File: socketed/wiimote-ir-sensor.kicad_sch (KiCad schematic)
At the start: 11 parts, among them J1 Conn_01x04_Pin, U2 AP2112-3.3V, X1 SG3225CAN 24.0000M-TJGA3

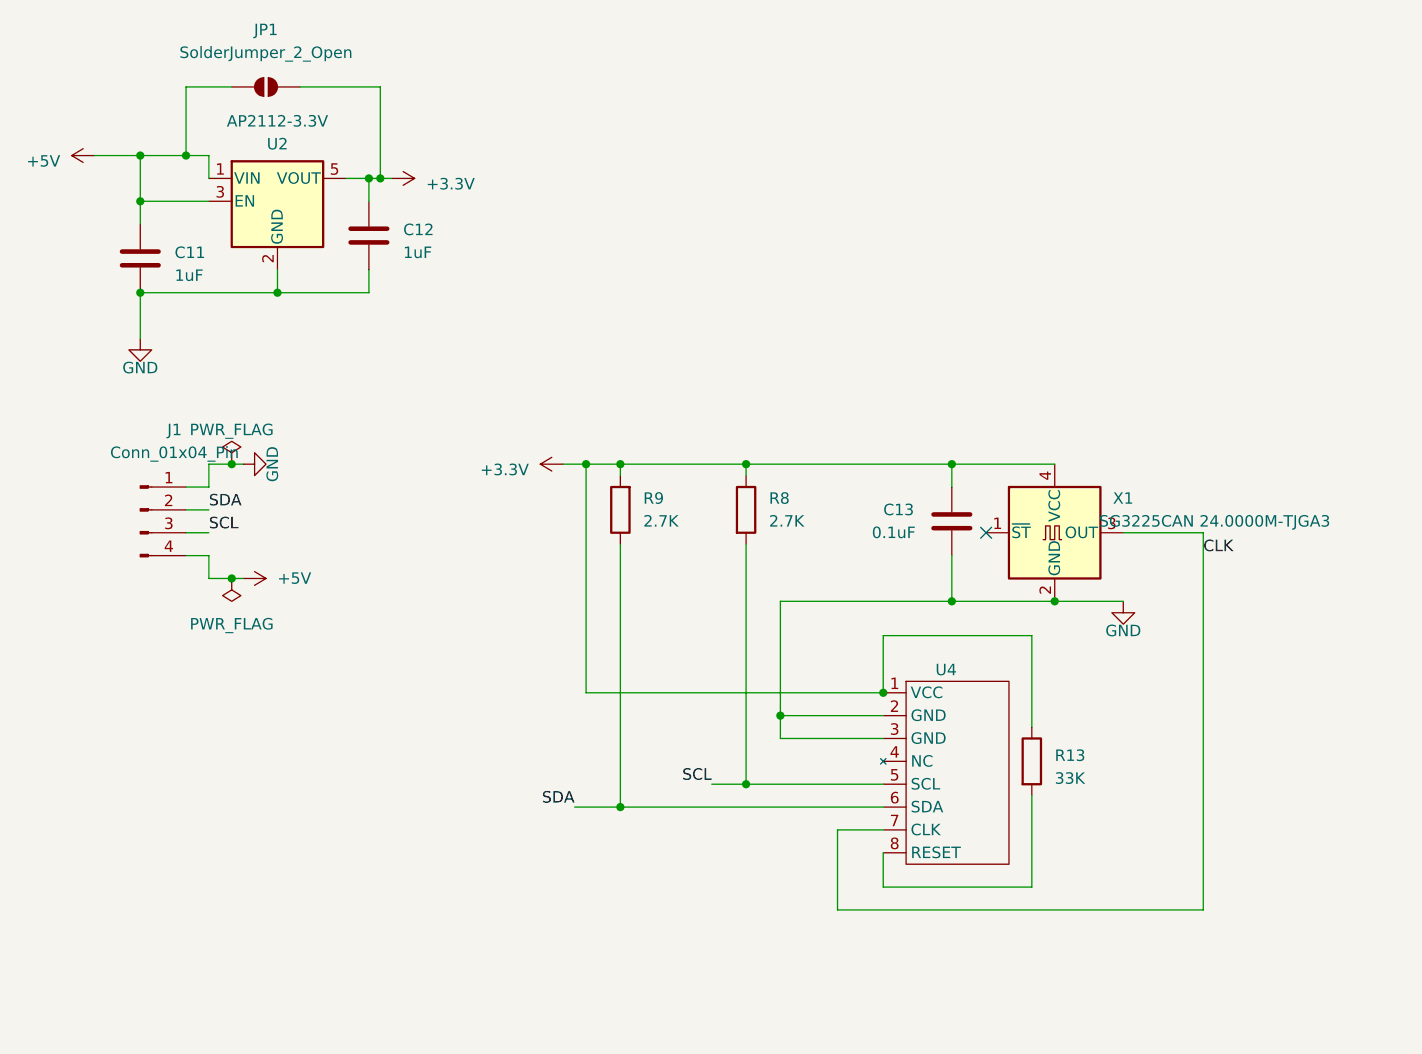
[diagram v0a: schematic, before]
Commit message: Cheaper PCBA (#3)
* Move all components to one side of the board for cheaper PCBA

* Socketed: Add option to wire CLK directly
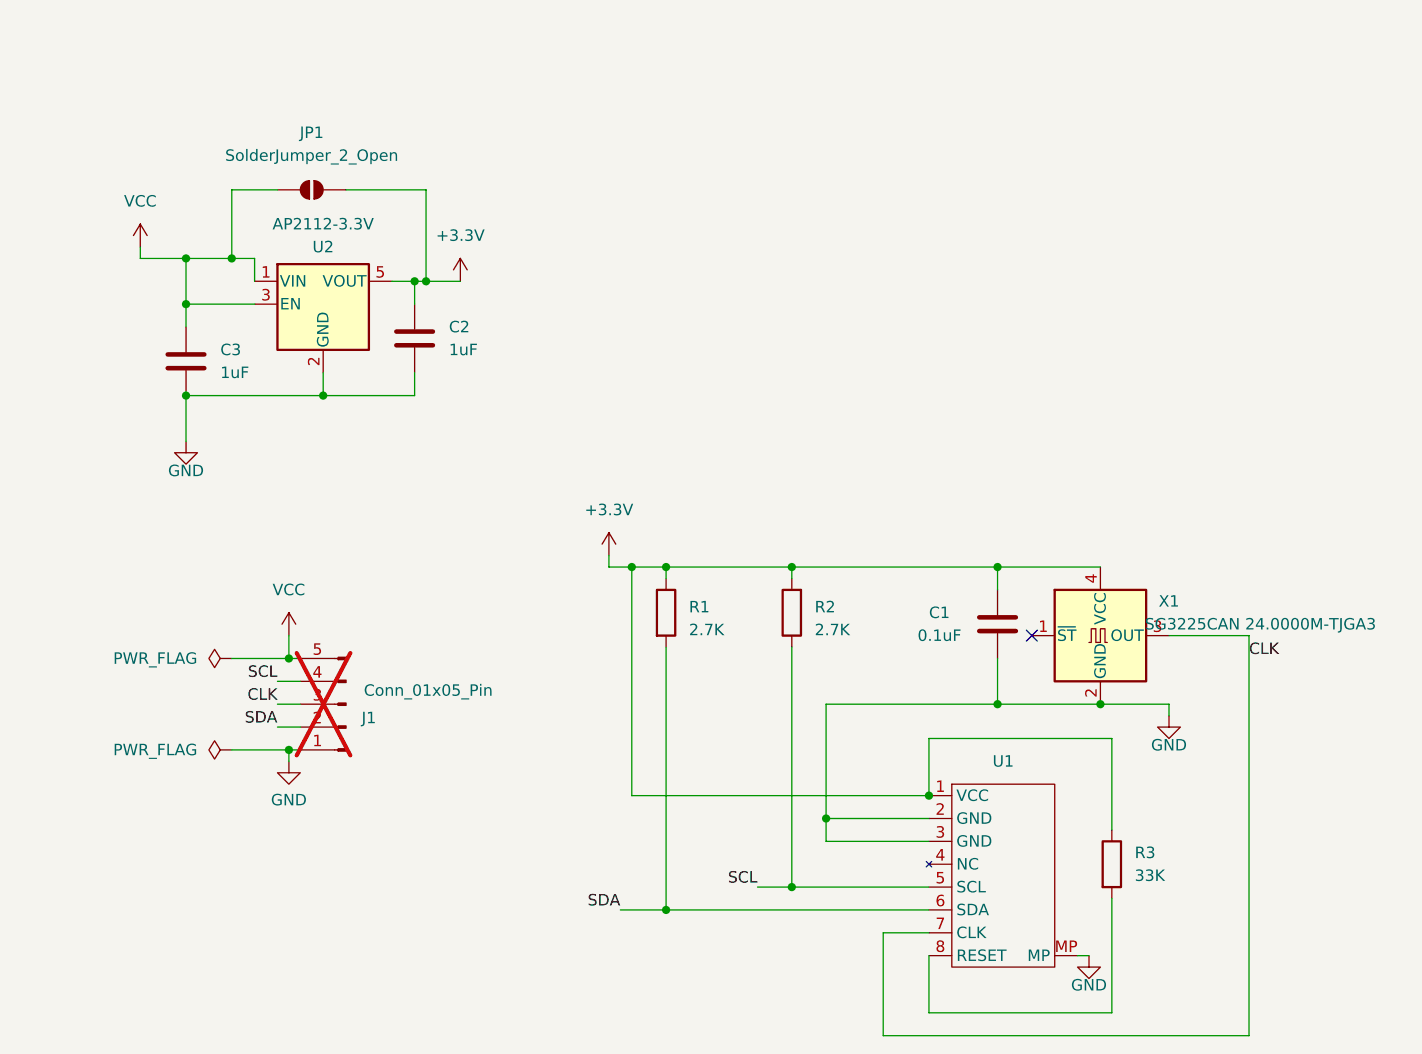
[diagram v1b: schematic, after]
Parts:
- removed C11, C12: 1uF, Capacitor_SMD:C_0603_1608Metric_Pad1.08x0.95mm_HandSolder, symbol Device:C
- removed C13: 0.1uF, Capacitor_SMD:C_0603_1608Metric_Pad1.08x0.95mm_HandSolder, symbol Device:C
- removed J1: Conn_01x04_Pin, Connector_PinHeader_2.54mm:PinHeader_1x04_P2.54mm_Vertical, symbol Connector:Conn_01x04_Pin
- removed R13: 33K, Resistor_SMD:R_0603_1608Metric_Pad0.98x0.95mm_HandSolder, symbol Device:R
- removed R8, R9: 2.7K, Resistor_SMD:R_0603_1608Metric_Pad0.98x0.95mm_HandSolder, symbol Device:R
- removed U4: ~, GUN4IR:wiimote-pixart-camera, symbol wiimote_ir_camera:Wiimote_IR_Camera
- added C1: 0.1uF, Capacitor_SMD:C_0603_1608Metric_Pad1.08x0.95mm_HandSolder, symbol Device:C
- added C2, C3: 1uF, Capacitor_SMD:C_0603_1608Metric_Pad1.08x0.95mm_HandSolder, symbol Device:C
- added J1: Conn_01x05_Pin, Connector_PinHeader_2.54mm:PinHeader_1x05_P2.54mm_Vertical, symbol Connector:Conn_01x05_Pin
- added R1, R2: 2.7K, Resistor_SMD:R_0603_1608Metric_Pad0.98x0.95mm_HandSolder, symbol Device:R
- added R3: 33K, Resistor_SMD:R_0603_1608Metric_Pad0.98x0.95mm_HandSolder, symbol Device:R
- added U1: (no value), wiimote-ir-sensor:wiimote-pixart-camera, symbol wiimote-ir-sensor:Wiimote_IR_Camera_MountingPoint
- U2: LCSC (none) -> C51118
- X1: LCSC (none) -> C5203548
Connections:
- net +3.3V: now also C1.1, C2.1, R1.1, R2.2, R3.1, U1.1 (VCC)
- net CLK: now also J1.3 (Pin_3), U1.7 (CLK)
- net GND: now also C1.2, C2.2, C3.2, J1.1 (Pin_1), U1.2 (GND), U1.3 (GND), U1.MP
- net SCL: now also J1.4 (Pin_4), R2.1, U1.5 (SCL)
- net SDA: now also J1.2 (Pin_2), R1.2, U1.6 (SDA)
- net +5V renamed VCC
- net VCC: now also C3.1, J1.5 (Pin_5)
- new net: R3.2, U1.8 (RESET)
